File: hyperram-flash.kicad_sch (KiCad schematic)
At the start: 17 parts, among them U1 IS66WVH16M8DALL-166B1LI, U27 W25Q128JWEIQ TR

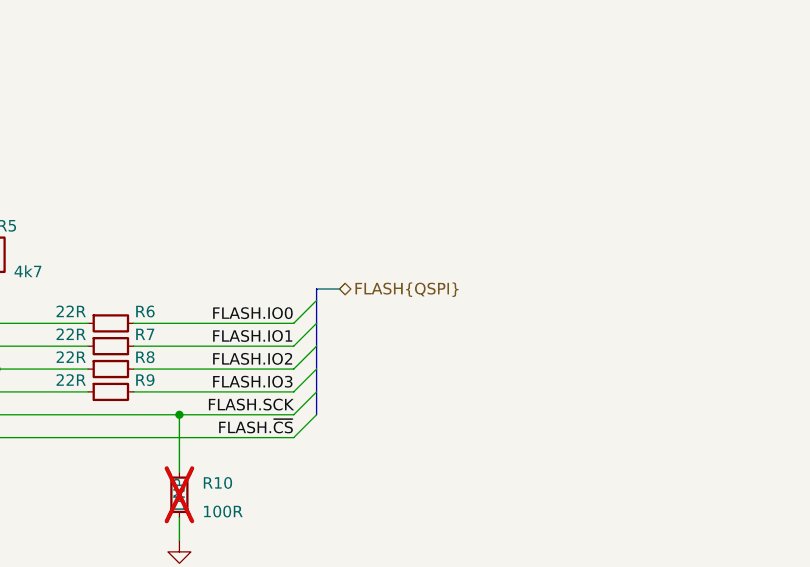
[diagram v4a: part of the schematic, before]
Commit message: [#68016] Improve bus entry marking
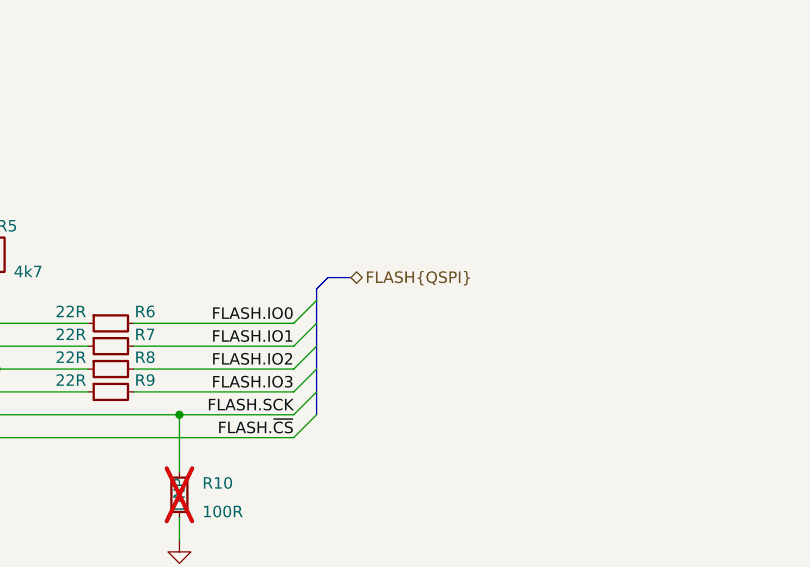
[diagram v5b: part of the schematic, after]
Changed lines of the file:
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@@
     (stroke (width 0) (type default))
   )
-  (bus (pts (xy 254 195.58) (xy 251.46 195.58))
+  (bus (pts (xy 255.27 194.31) (xy 252.73 194.31))
     (stroke (width 0) (type default))
   )
@@
   )
   (wire (pts (xy 199.39 212.09) (xy 199.39 194.31))
+    (stroke (width 0) (type default))
+  )
+  (bus (pts (xy 251.46 195.58) (xy 252.73 194.31))
     (stroke (width 0) (type default))
   )
@@
     (effects (font (size 1.27 1.27)) (justify left bottom))
   )
-  (hierarchical_label "FLASH{QSPI}" (shape bidirectional) (at 254 195.58 0) (fields_autoplaced)
+  (hierarchical_label "FLASH{QSPI}" (shape bidirectional) (at 255.27 194.31 0) (fields_autoplaced)
     (effects (font (size 1.27 1.27)) (justify left))
   )

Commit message: [#68016] Solve ERC warrings and errors
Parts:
- removed U27: W25Q128JWEIQ TR, antmicro-footprints:WSON-8_6x8x0.5mm_P1.27mm, symbol antmicroMemory:W25Q128JWEIQ TR
- added U27: W25Q128JWEIQ, antmicro-footprints:WSON-8_6x8x0.5mm_P1.27mm, symbol antmicroMemory:W25Q128JWEIQ
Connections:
- net +1V8: now also U27.8 (V_{CC})
- net FLASH.SCK: now also U27.6 (SCK)
- net FLASH.~{CS}: now also U27.1 (~{CS})
- net GND: now also U27.4 (V_{SS})
- net IO0: now also U27.5 (DI/IO0)
- net IO1: now also U27.2 (DO/IO1)
- net IO2: now also U27.3 (~{WP}/IO2)
- net IO3: now also U27.7 (~{HOLD}/IO3)
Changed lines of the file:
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@@
+    )
+  )
+  (symbol (lib_id "antmicroMemory:W25Q128JWEIQ") (at 189.23 199.39 0) (mirror y) (unit 1)
+    (in_bom yes) (on_board yes) (dnp no)
+    (property "Reference" "U27" (at 179.07 191.77 0)
+      (effects (font (size 1.27 1.27) (thickness 0.15)))
+    )
+    (property "Value" "W25Q128JWEIQ" (at 148.59 207.01 0)
+      (effects (font (size 1.27 1.27) (thickness 0.15)) (justify left bottom) hide)
+    )
+    (property "Footprint" "antmicro-footprints:WSON-8_6x8x0.5mm_P1.27mm" (at 148.59 209.55 0)
+      (effects (font (size 1.27 1.27) (thickness 0.15)) (justify left bottom) hide)
+    )
+    (property "Datasheet" "https://www.winbond.com/resource-files/W25Q128JW_RevG_07292021%20Plus.pdf" (at 148.59 212.09 0)
+      (effects (font (size 1.27 1.27) (thickness 0.15)) (justify left bottom) hide)
+    )
+    (property "Manufacturer" "Winbond" (at 148.59 214.63 0)
+      (effects (font (size 1.27 1.27) (thickness 0.15)) (justify left bottom) hide)
+    )
+    (property "MPN" "W25Q128JWEIQ TR" (at 179.07 194.31 0)
+      (effects (font (size 1.27 1.27) (thickness 0.15)))
+    )
+    (property "Author" "Antmicro" (at 148.59 217.17 0)
+      (effects (font (size 1.27 1.27) (thickness 0.15)) (justify left bottom) hide)
+    )
+    (property "License" "Apache-2.0" (at 148.59 219.71 0)
+      (effects (font (size 1.27 1.27) (thickness 0.15)) (justify left bottom) hide)
+    )
+    (pin "7")
+    (pin "3")
+    (pin "4")
+    (pin "1")
+    (pin "2")
+    (pin "6")
+    (pin "9")
+    (pin "5")
+    (pin "8")
+    (instances
+      (project "data-center-rdimm-ddr5-tester"
+        (path "/1faa6543-e26a-4449-8bac-ee14b9f19e5f/00000000-0000-0000-0000-00005fea2994"
+          (reference "U27") (unit 1)
+        )
+      )
     )
   )
@@
         )
       )
-    )
-  )
-  (symbol (lib_id "antmicroMemory:W25Q128JWEIQ TR") (at 189.23 199.39 0) (mirror y) (unit 1)
-    (in_bom yes) (on_board yes) (dnp no) (fields_autoplaced)
-    (property "Reference" "U27" (at 179.07 191.77 0)
-      (effects (font (size 1.27 1.27) (thickness 0.15)))
-    )
-    (property "Value" "W25Q128JWEIQ TR" (at 148.59 207.01 0)
-      (effects (font (size 1.27 1.27) (thickness 0.15)) (justify left bottom) hide)
-    )
-    (property "Footprint" "antmicro-footprints:WSON-8_6x8x0.5mm_P1.27mm" (at 148.59 209.55 0)
-      (effects (font (size 1.27 1.27) (thickness 0.15)) (justify left bottom) hide)
-    )
-    (property "Datasheet" "https://www.winbond.com/resource-files/W25Q128JW_RevG_07292021%20Plus.pdf" (at 148.59 212.09 0)
-      (effects (font (size 1.27 1.27) (thickness 0.15)) (justify left bottom) hide)
-    )
-    (property "Manufacturer" "Winbond Electronics" (at 148.59 214.63 0)
-      (effects (font (size 1.27 1.27) (thickness 0.15)) (justify left bottom) hide)
-    )
-    (property "MPN" "W25Q128JWEIQ TR" (at 179.07 194.31 0)
-      (effects (font (size 1.27 1.27) (thickness 0.15)))
-    )
-    (property "Author" "Antmicro" (at 148.59 217.17 0)
-      (effects (font (size 1.27 1.27) (thickness 0.15)) (justify left bottom) hide)
-    )
-    (property "License" "Apache-2.0" (at 148.59 219.71 0)
-      (effects (font (size 1.27 1.27) (thickness 0.15)) (justify left bottom) hide)
-    )
-    (pin "5")
-    (pin "1")
-    (pin "6")
-    (pin "2")
-    (pin "9")
-    (pin "3")
-    (pin "8")
-    (pin "7")
-    (pin "4")
-    (instances
-      (project "data-center-rdimm-ddr5-tester"
-        (path "/1faa6543-e26a-4449-8bac-ee14b9f19e5f/00000000-0000-0000-0000-00005fea2994"
-          (reference "U27") (unit 1)
-        )
-      )
